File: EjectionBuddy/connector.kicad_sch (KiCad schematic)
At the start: 12 parts, among them J10 Conn_01x04, J11 Conn_01x04, J12 Conn_01x04, J13 Conn_01x04, J14 Conn_01x02, J3 Conn_01x04, J4 Conn_01x08, J5 Conn_01x04, J6 Conn_01x04, J7 Conn_01x04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

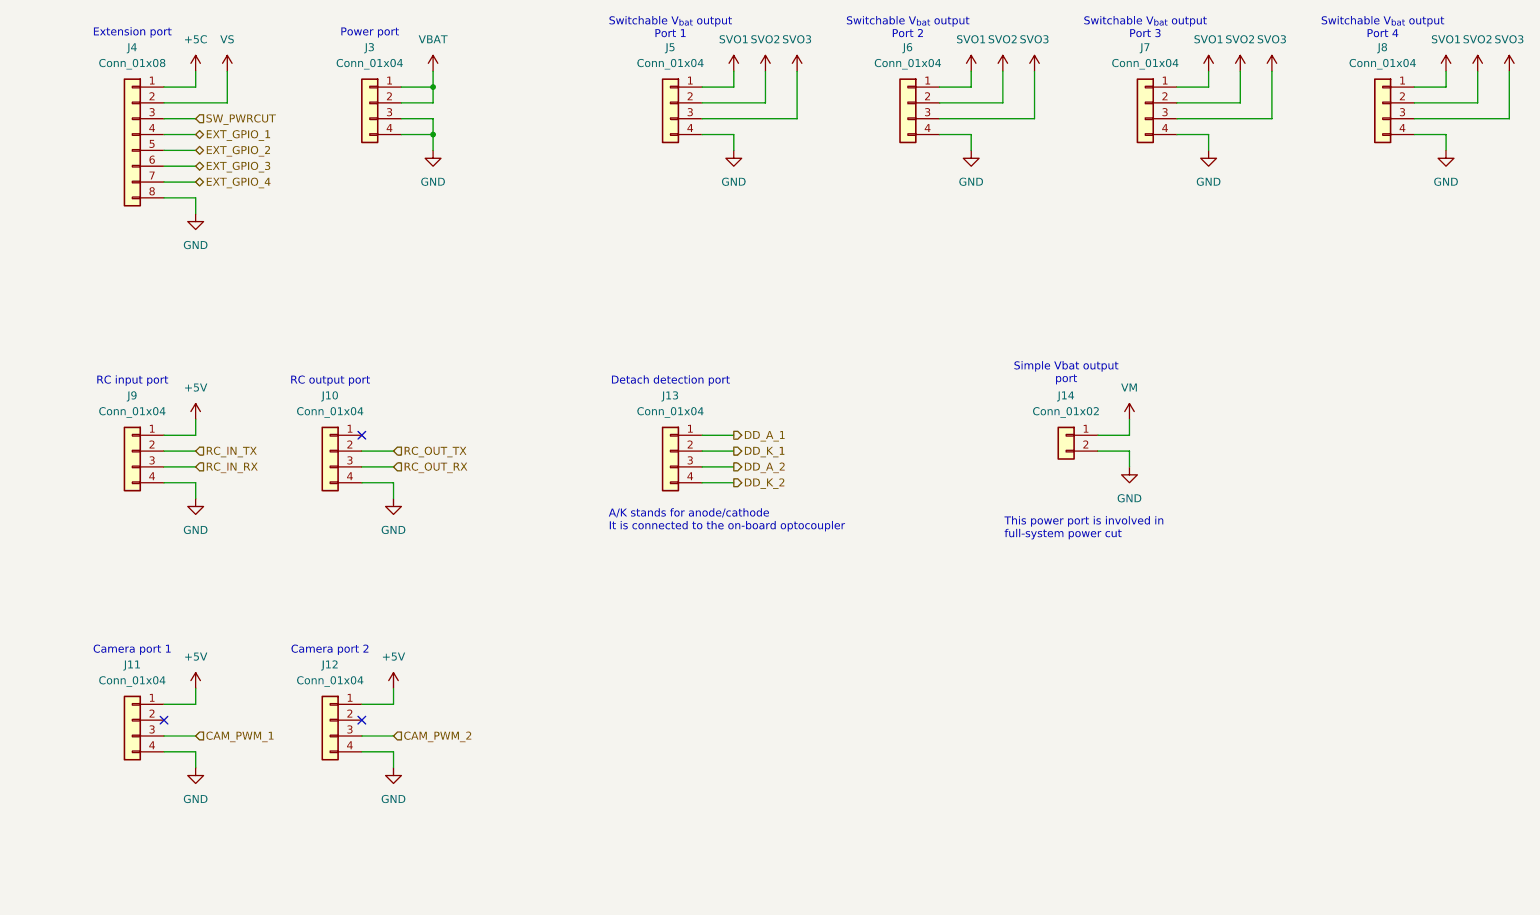
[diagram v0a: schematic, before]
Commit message: Untrack sch renaming poop and renamed connecter.sch to connector.sch
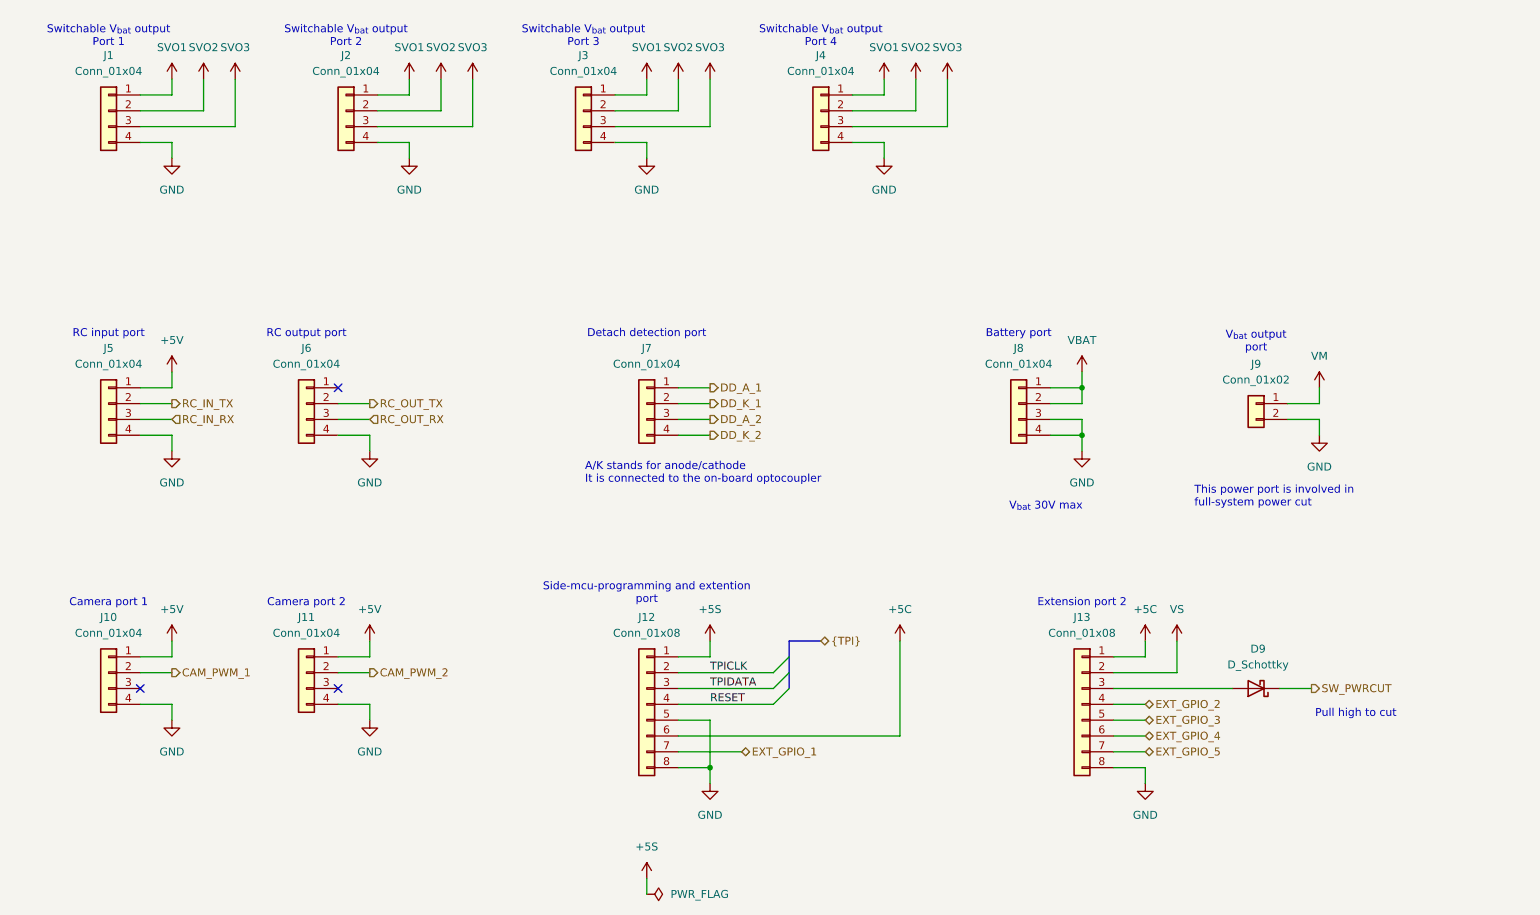
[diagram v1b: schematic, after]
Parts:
- added D9: D_Schottky, Diode_SMD:D_SOD-523, symbol Device:D_Schottky
- added J12: Conn_01x08, Connector_JST:JST_GH_SM08B-GHS-TB_1x08-1MP_P1.25mm_Horizontal, symbol Connector_Generic:Conn_01x08
- J1: renamed from J5; footprint (none) -> Connector_JST:JST_GH_SM04B-GHS-TB_1x04-1MP_P1.25mm_Horizontal
- J10: renamed from J11; footprint (none) -> Connector_JST:JST_GH_SM04B-GHS-TB_1x04-1MP_P1.25mm_Horizontal
- J11: renamed from J12; footprint (none) -> Connector_JST:JST_GH_SM04B-GHS-TB_1x04-1MP_P1.25mm_Horizontal
- J13: renamed from J4; footprint (none) -> Connector_JST:JST_GH_SM08B-GHS-TB_1x08-1MP_P1.25mm_Horizontal
- J2: renamed from J6; footprint (none) -> Connector_JST:JST_GH_SM04B-GHS-TB_1x04-1MP_P1.25mm_Horizontal
- J3: renamed from J7; footprint (none) -> Connector_JST:JST_GH_SM04B-GHS-TB_1x04-1MP_P1.25mm_Horizontal
- J4: renamed from J8; footprint (none) -> Connector_JST:JST_GH_SM04B-GHS-TB_1x04-1MP_P1.25mm_Horizontal
- J5: renamed from J9; footprint (none) -> Connector_JST:JST_GH_SM04B-GHS-TB_1x04-1MP_P1.25mm_Horizontal
- J6: renamed from J10; footprint (none) -> Connector_JST:JST_GH_SM04B-GHS-TB_1x04-1MP_P1.25mm_Horizontal
- J7: renamed from J13; footprint (none) -> Connector_JST:JST_GH_SM04B-GHS-TB_1x04-1MP_P1.25mm_Horizontal
- J8: renamed from J3; footprint (none) -> Connector_JST:JST_GH_SM04B-GHS-TB_1x04-1MP_P1.25mm_Horizontal
- J9: renamed from J14; footprint (none) -> Connector_JST:JST_GH_SM02B-GHS-TB_1x02-1MP_P1.25mm_Horizontal
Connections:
- net +5C: now also J12.6 (Pin_6)
- net CAM_PWM_1: now also J10.2 (Pin_2); no longer J10.3 (Pin_3)
- net CAM_PWM_2: now also J11.2 (Pin_2); no longer J11.3 (Pin_3)
- net EXT_GPIO_1: now also J12.7 (Pin_7); no longer J13.4 (Pin_4)
- net EXT_GPIO_2: now also J13.4 (Pin_4); no longer J13.5 (Pin_5)
- net EXT_GPIO_3: now also J13.5 (Pin_5); no longer J13.6 (Pin_6)
- net EXT_GPIO_4: now also J13.6 (Pin_6); no longer J13.7 (Pin_7)
- net GND: now also J12.5 (Pin_5), J12.8 (Pin_8)
- net SW_PWRCUT: now also D9.1 (K); no longer J13.3 (Pin_3)
- new net: D9.2 (A), J13.3 (Pin_3)
- new net +5S: J12.1 (Pin_1)
- new net EXT_GPIO_5: J13.7 (Pin_7)
- new net RESET: J12.4 (Pin_4)
- new net TPICLK: J12.2 (Pin_2)
- new net TPIDATA: J12.3 (Pin_3)
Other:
- note added: "Battery port"
- note added: "Extension port 2"
- note added: "Pull high to cut"
- note added: "Side-mcu-programming and extention port"
- note added: "V_{bat} 30V max"
- note added: "V_{bat} output port"
- note removed: "Extension port"
- note removed: "Power port"
- note removed: "Simple Vbat output port"
- moved on the sheet: J1, J10, J11, J13, J2, J3, J4, J5, J6, J7, J8, J9
